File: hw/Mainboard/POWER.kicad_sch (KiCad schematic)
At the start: 66 parts, among them J1 9V POWER, J2 9V POWER, J3 PET POWER, J4 5V PWR, U3 LM317AG-TN3-R, U4 XL1509-5.0E1, U5 LM317AG-TN3-R, U6 AMS1117-3.3

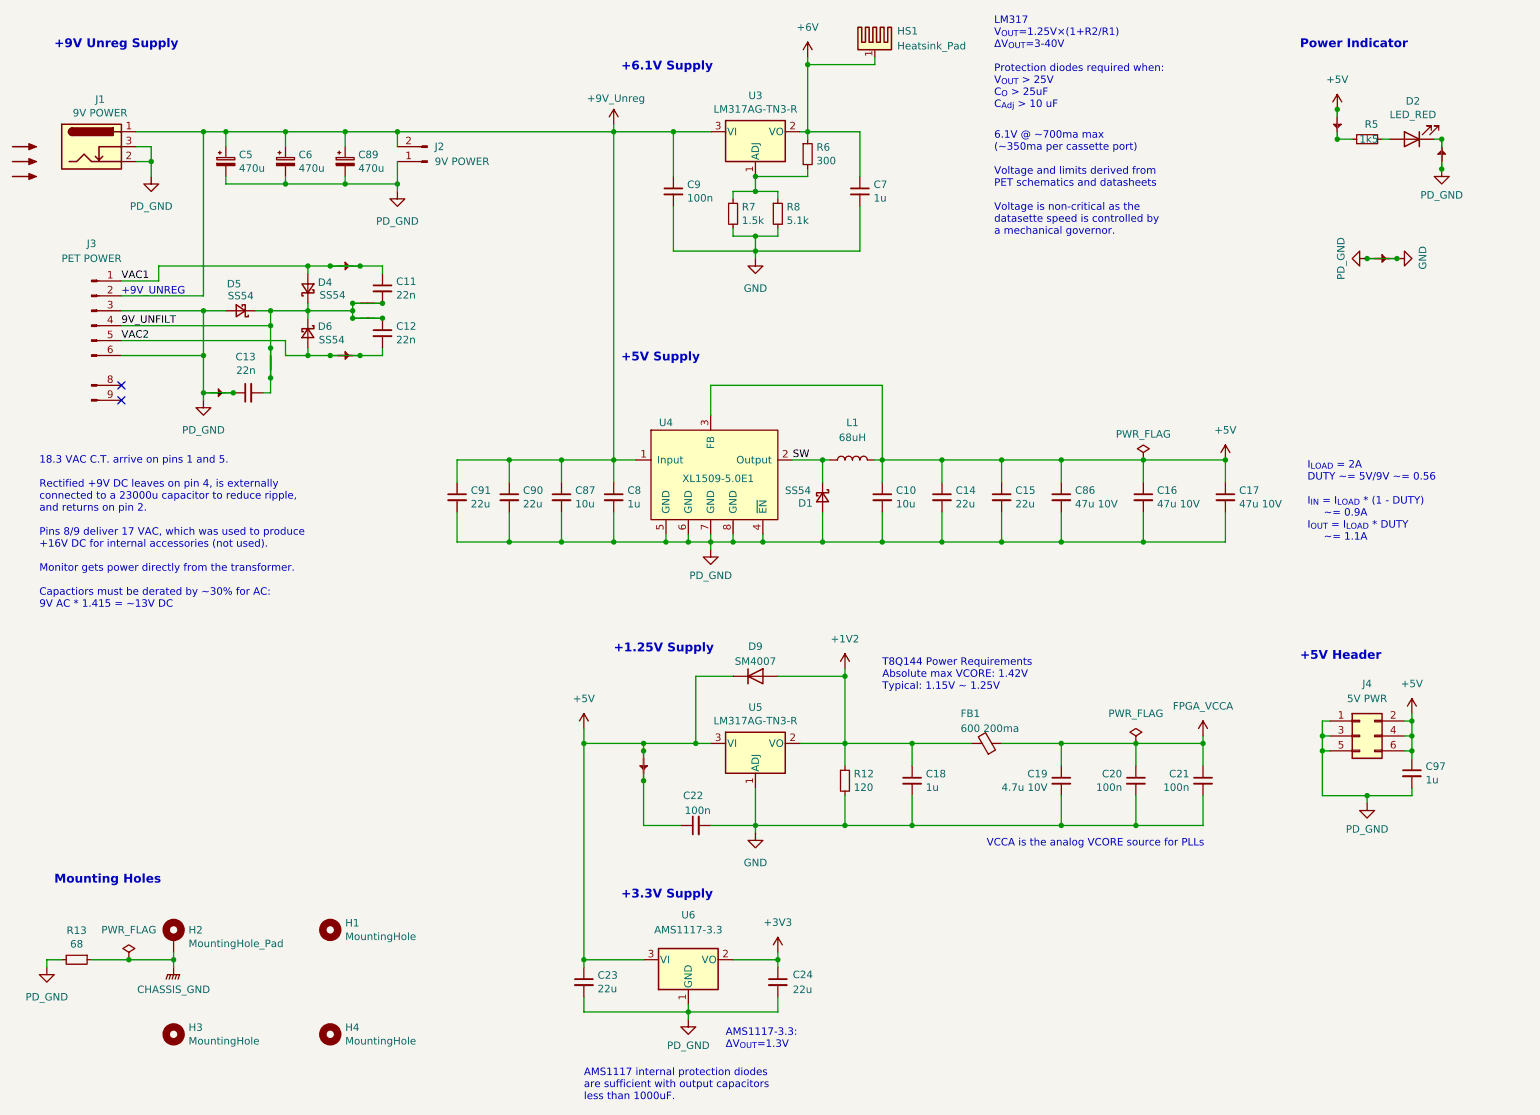
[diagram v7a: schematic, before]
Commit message: hw: remove net/power ties
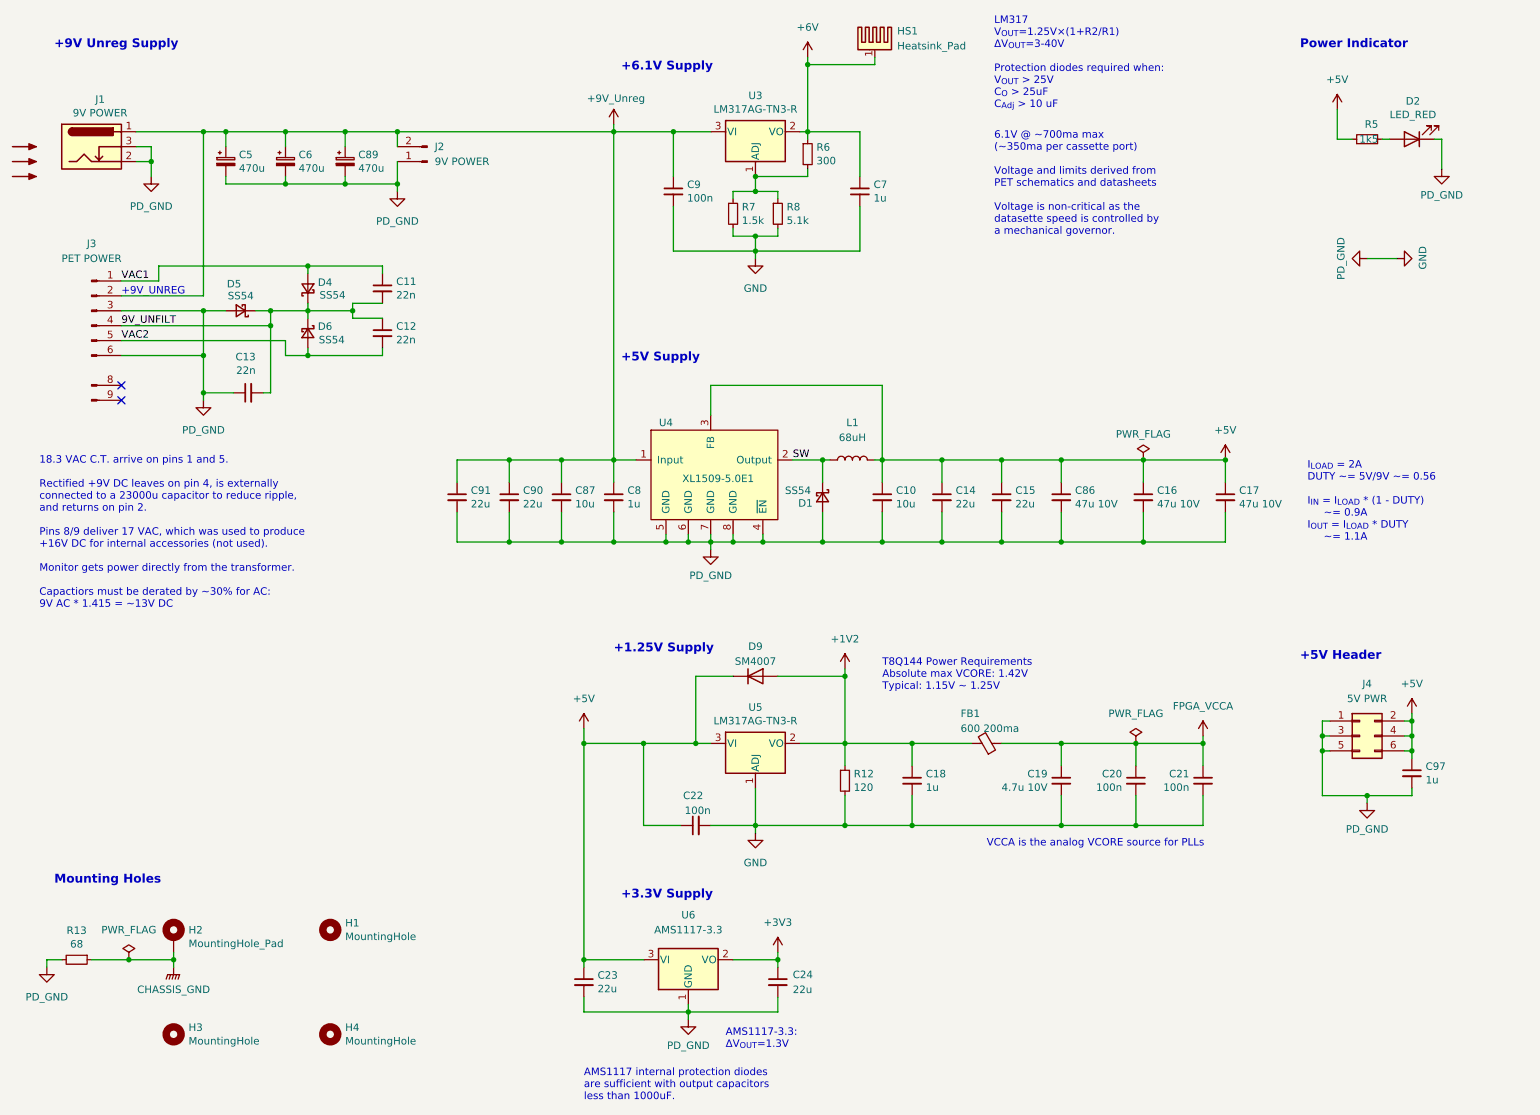
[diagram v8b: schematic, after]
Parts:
- removed PT10, PT11, PT12, PT2, PT4, PT5, PT8: PowerTie_2, PET:NetTie-2_SMD_Pad_1.6_to_0.4mm, symbol PET:PowerTie_2
- removed PT6, PT7, PT9: PowerTie_2, PET:NetTie-2_SMD_Pad_1.6_to_0.4mm, symbol Device:NetTie_2
